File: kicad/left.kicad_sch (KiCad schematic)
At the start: 118 parts, among them Q1 PMF170XP,115, Q2 FS8205A_C2830320, SW1 TS-1088-AR02016, U1 TLV7031QDCKRQ1, U2 E73-2G4M08S1C, U3 SN74LVC1G74DQER, U4 S2B-PH-K-S(LF)(SN), U5 BL8573CS8TR, U6 DW01A_C42380662, U7 LP5024RSMR, X1 FC-13532.768KHZ9PF20PPM

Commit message: ...
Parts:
- added R17: RC0402FR-071ML, easyeda2kicad:R0402, symbol easyeda2kicad:RC0402FR-071ML
- added R18: WR04W2494FTL, easyeda2kicad:R0402, symbol easyeda2kicad:WR04W2494FTL
- S1, S10, S11, S12, S13, S14, S15, S16, S17, S18, S19, S2, S20, S3, S4, S5, S6, S7, S8, S9: footprint hexcaps:PG1350_hotswap -> hexcaps:PG1350_hotswap_reversed
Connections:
- net COL6 is gone; now on net LED_SCL: U2.17 (P1.09)
- net COL7 is gone; now on net STDBY: U2.1 (P1.11)
- net CHRG: now also U2.2 (P1.10); no longer U2.43 (NF2)
- net COL1: now also U2.32 (P0.20); no longer U2.38 (P1.02)
- net COL2: now also U2.34 (P0.22); no longer U2.36 (P1.00)
- net COL3: now also U2.36 (P1.00); no longer U2.34 (P0.22)
- net COL4: now also U2.38 (P1.02); no longer U2.32 (P0.20)
- net COL5: now also U2.40 (P1.04); no longer U2.6 (P1.13)
- net GND: now also R18.1
- net LED1: now also U7.8 (OUT7); no longer U7.17 (OUT16)
- net LED10: now also U7.18 (OUT17); no longer U7.7 (OUT6)
- net LED11: now also U7.22 (OUT21); no longer U7.3 (OUT2)
- net LED12: now also U7.5 (OUT4); no longer U7.20 (OUT19)
- net LED13: now also U7.11 (OUT10); no longer U7.14 (OUT13)
- net LED14: now also U7.19 (OUT18); no longer U7.6 (OUT5)
- net LED15: now also U7.23 (OUT22); no longer U7.2 (OUT1)
- net LED16: now also U7.4 (OUT3); no longer U7.21 (OUT20)
- net LED17: now also U7.10 (OUT9); no longer U7.15 (OUT14)
- net LED18: now also U7.20 (OUT19); no longer U7.5 (OUT4)
- net LED19: now also U7.24 (OUT23); no longer U7.1 (OUT0)
- net LED2: now also U7.14 (OUT13); no longer U7.11 (OUT10)
- net LED20: now also U7.1 (OUT0); no longer U7.24 (OUT23)
- net LED3: now also U7.15 (OUT14); no longer U7.10 (OUT9)
- net LED4: now also U7.7 (OUT6); no longer U7.18 (OUT17)
- net LED5: now also U7.13 (OUT12); no longer U7.12 (OUT11)
- net LED6: now also U7.17 (OUT16); no longer U7.8 (OUT7)
- net LED7: now also U7.21 (OUT20); no longer U7.4 (OUT3)
- net LED8: now also U7.6 (OUT5); no longer U7.19 (OUT18)
- net LED9: now also U7.12 (OUT11); no longer U7.13 (OUT12)
- net LED_EN: now also U2.15 (AI3); no longer U2.7 (AI0)
- net LED_SCL: no longer U2.9 (AI7)
- net LED_SDA: now also U2.16 (P0.08); no longer U2.8 (AI5)
- net PWR_BTN: now also R17.2
- net ROW1: now also U2.9 (AI7); no longer U2.28 (P15)
- net ROW3: now also U2.33 (P0.13); no longer U2.12 (P0.26)
- net ROW4: now also U2.42 (P1.06)
- net STDBY: no longer U2.41 (NF1)
- net SWBCLK: now also U2.37 (SWD); no longer U2.39 (SWC)
- net SWDIO: now also U2.39 (SWC); no longer U2.37 (SWD)
- net PWR_BTN_PRESS: now reaches U2.3 (P0.03)
- net PWR_BTN_PRESS: now also R17.1, R18.2

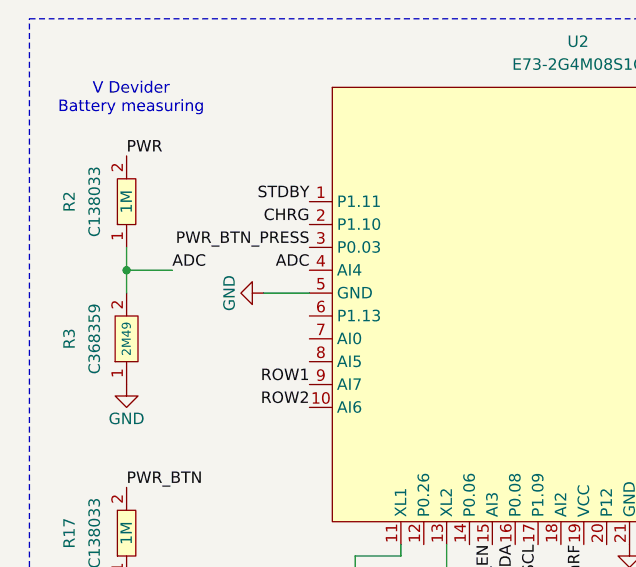
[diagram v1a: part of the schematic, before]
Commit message: left wiring done... right changed to shmitt inctead of comparator... need to do same on left... fixing of right in progress
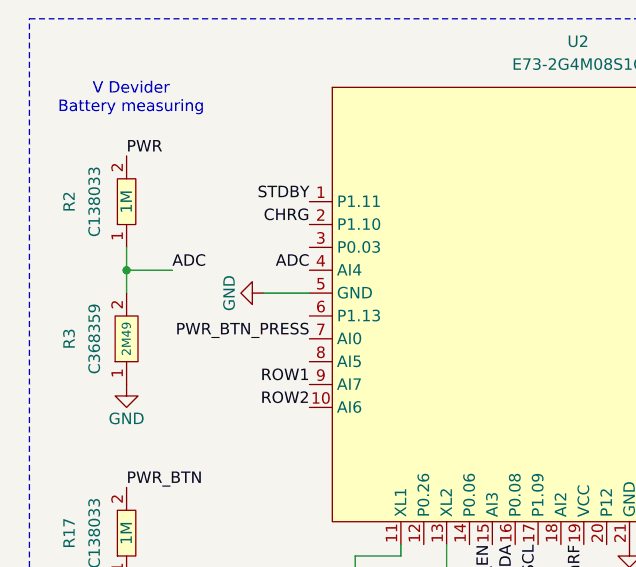
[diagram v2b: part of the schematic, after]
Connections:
- net PWR_BTN_PRESS: now also U2.7 (AI0); no longer U2.3 (P0.03)
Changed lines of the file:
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@@
+		)
+	)
+	(label "PWR_BTN_PRESS"
+		(at 45.72 123.19 180)
+		(effects
+			(font
+				(size 1.27 1.27)
+			)
+			(justify right bottom)
 		)
 	)
@@
 		(effects
 			(font
-				(size 1.27 1.27)
-			)
-			(justify right bottom)
-		)
-	)
-	(label "PWR_BTN_PRESS"
-		(at 45.72 113.03 180)
-		(effects
-			(font

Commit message: pcb done. schematick done. need to double check schematick and ask in discord about pcb... but else done
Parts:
- removed R5: RC0402FR-074M3L, :R0402, symbol easyeda2kicad:RC0402FR-074M3L
- removed R6: RC0402FR-071ML, easyeda2kicad:R0402, symbol easyeda2kicad:RC0402FR-071ML
- removed U1: TLV7031QDCKRQ1, :SC-70-5_L2.0-W1.3-P0.65-LS2.1-BR, symbol easyeda2kicad:TLV7031QDCKRQ1
- added U1: SN74LVC1G17DBVR, easyeda2kicad:SOT-23-5_L3.0-W1.7-P0.95-LS2.8-BR, symbol easyeda2kicad:SN74LVC1G17DBVR
- renumbered R17 to R4, R18 to R5, R4 to R6
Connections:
- net GND: now also U1.3 (GND)
- net PWR_BTN: now also U1.5 (VCC)
- net at C2.1, D1.2, R6.2: now also U1.2 (A)
- net at U3.1 (CLK): now also U1.4 (Y)
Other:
- moved on the sheet: U3

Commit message: text position changes
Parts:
- removed R6: WR04W2494FTL, easyeda2kicad:R0402, symbol easyeda2kicad:WR04W2494FTL
- added R6: 0402WGF1604TCE, easyeda2kicad:R0402, symbol easyeda2kicad:0402WGF1604TCE
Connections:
- net PWR_BTN: now also R6.1
- net at C2.1, D1.2, U1.2 (A): now also R6.2
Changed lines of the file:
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@@
 	)
 	(symbol
-		(lib_id "easyeda2kicad:WR04W2494FTL")
-		(at 36.83 39.37 0)
-		(unit 1)
-		(exclude_from_sim no)
-		(in_bom yes)
-		(on_board yes)
-		(dnp no)
-		(property "Reference" "R6"
-			(at 36.83 33.02 0)
-			(effects
-				(font
-					(size 1.27 1.27)
-				)
-			)
-		)
-		(property "Value" "WR04W2494FTL"
-			(at 36.83 35.56 0)
-			(effects
-				(font
-					(size 1.27 1.27)
-				)
-				(hide yes)
-			)
-		)
-		(property "Footprint" "easyeda2kicad:R0402"
-			(at 36.83 46.99 0)
-			(effects
-				(font
-					(size 1.27 1.27)
-				)
-				(hide yes)
-			)
-		)
-		(property "Datasheet" "https://lcsc.com/product-detail/Others_Walsin-Tech-Corp-WR04W2494FTL_C368359.html"
-			(at 36.83 49.53 0)
-			(effects
-				(font
-					(size 1.27 1.27)
-				)
-				(hide yes)
-			)
-		)
-		(property "Description" "2M49"
-			(at 36.83 39.37 0)
-			(effects
-				(font
-					(size 1 1)
-				)
-			)
-		)
-		(property "LCSC Part" "C368359"
-			(at 36.83 35.814 0)
-			(effects
-				(font
-					(size 1.27 1.27)
-				)
-			)
-		)
-		(pin "1"
-		)
-		(pin "2"
-		)
-		(instances
-			(project ""
-				(path "/3171f1b4-f2dd-4471-8b63-415e18370dba"
-					(reference "R6")
-					(unit 1)
-				)
-			)
-		)
-	)
-	(symbol
 		(lib_id "PCM_SparkFun-PowerSymbol:GND")
 		(at 168.91 35.56 270)
@@
 					(unit 1)
 				)
+			)
+		)
+	)
+	(symbol
+		(lib_id "easyeda2kicad:0402WGF1604TCE")
+		(at 36.83 39.37 0)
+		(unit 1)
+		(exclude_from_sim no)
+		(in_bom yes)
+		(on_board yes)
+		(dnp no)
+		(property "Reference" "R6"
+			(at 36.83 36.83 0)
+			(effects
+				(font
+					(size 1.27 1.27)
+				)
+			)
+		)
+		(property "Value" "0402WGF1604TCE"
+			(at 36.83 35.56 0)
+			(effects
+				(font
+					(size 1.27 1.27)
+				)
+				(hide yes)
+			)
+		)
+		(property "Footprint" "easyeda2kicad:R0402"
+			(at 36.83 46.99 0)
+			(effects
+				(font
+					(size 1.27 1.27)
+				)
+				(hide yes)
+			)
+		)
+		(property "Datasheet" "https://lcsc.com/product-detail/Chip-Resistor-Surface-Mount_Uniroyal-Elec-0402WGF1604TCE_C423231.html"
+			(at 36.83 49.53 0)
+			(effects
+				(font
+					(size 1.27 1.27)
+				)
+				(hide yes)
+			)
+		)
+		(property "Description" "3M48"
+			(at 36.83 39.37 0)
+			(effects
+				(font
+					(size 1.016 1.016)
+				)
+			)
+		)
+		(property "LCSC Part" "C423231"
+			(at 36.83 52.07 0)
+			(effects
+				(font
+					(size 1.27 1.27)
+				)
+				(hide yes)
+			)
+		)
+		(pin "2"
+		)
+		(pin "1"
+		)
+		(instances
+			(project "left"
+				(path "/3171f1b4-f2dd-4471-8b63-415e18370dba"
+					(reference "R6")
+					(unit 1)
+				)

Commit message: checked and update schematics on off need to update it in pcb...
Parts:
- removed R1: RC0402FR-07100KL, easyeda2kicad:R0402, symbol easyeda2kicad:RC0402FR-07100KL
- added C4: GRM033C71C104KE14D, easyeda2kicad:C0201, symbol easyeda2kicad:GRM033C71C104KE14D
- added R5, R7: RC0402FR-07100KL, easyeda2kicad:R0402, symbol easyeda2kicad:RC0402FR-07100KL
- renumbered C9 to C10, C10 to C11, C11 to C12, C12 to C13, C13 to C14, C14 to C15, C15 to C16, C16 to C17, C17 to C18, C18 to C19, C19 to C20, C20 to C21, C21 to C22, C22 to C23, C23 to C24, C24 to C25, C25 to C26, C26 to C27, C27 to C28, C4 to C5, C5 to C6, C6 to C7, C7 to C8, C8 to C9, R2 to R1, R9 to R10, R10 to R11, R11 to R12, R12 to R13, R13 to R14, R14 to R15, R15 to R16, R16 to R17, R3 to R2, R4 to R3, R5 to R4, R7 to R8, R8 to R9
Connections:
- net BAT+: now also U1.5 (VCC), R7.2; no longer U3.6 (~{CLR})
- net GND: now also C4.1, R5.2
- net PWR_BTN: now also R5.1; no longer U1.5 (VCC)
- new net: C4.2, R7.1, U3.6 (~{CLR})
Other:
- moved on the sheet: C2, D1, U1, U3

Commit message: .
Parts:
- removed C10, C11, C12, C13, C14, C15, C16, C17, C18, C19, C20, C21, C22, C23, C24, C25, C26, C7, C8, C9: GRM033C71C104KE14D, easyeda2kicad:C0201, symbol easyeda2kicad:GRM033C71C104KE14D
- removed C6: GRM188C71C475KE21D, easyeda2kicad:C0603, symbol easyeda2kicad:GRM188C71C475KE21D
- removed R7: RC0402FR-07100KL, easyeda2kicad:R0402, symbol easyeda2kicad:RC0402FR-07100KL
- added C6: ZRB15XR61A475KE01D, easyeda2kicad:C0402, symbol easyeda2kicad:ZRB15XR61A475KE01D
- added R18: RC0402FR-0710KL, easyeda2kicad:R0402, symbol easyeda2kicad:RC0402FR-0710KL
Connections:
- net BAT+: now also R18.2
- net GND: now also C6.2
- net VBUS: now also C6.1
- net at C4.2, U3.6 (~{CLR}): now also R18.1

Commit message: .
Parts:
- removed C6: ZRB15XR61A475KE01D, easyeda2kicad:C0402, symbol easyeda2kicad:ZRB15XR61A475KE01D
- removed R18: RC0402FR-0710KL, easyeda2kicad:R0402, symbol easyeda2kicad:RC0402FR-0710KL
- removed R3: RC0402FR-071ML, easyeda2kicad:R0402, symbol easyeda2kicad:RC0402FR-071ML
- removed R4: WR04W2494FTL, easyeda2kicad:R0402, symbol easyeda2kicad:WR04W2494FTL
- removed R5: RC0402FR-07100KL, easyeda2kicad:R0402, symbol easyeda2kicad:RC0402FR-07100KL
- added C5: ZRB15XR61A475KE01D, easyeda2kicad:C0402, symbol easyeda2kicad:ZRB15XR61A475KE01D
- added C9: GRM033C71C104KE14D, easyeda2kicad:C0201, symbol easyeda2kicad:GRM033C71C104KE14D
- added R3: RC0402FR-07100KL, easyeda2kicad:R0402, symbol easyeda2kicad:RC0402FR-07100KL
- added R4, R7: RC0402FR-0710KL, easyeda2kicad:R0402, symbol easyeda2kicad:RC0402FR-0710KL
- added U8: MAX17048, PCM_SparkFun-Semiconductor-Standard:DFN-8_2x2mm_P0.5mm_EP1.2x0.8mm, symbol PCM_SparkFun-IC-Power:MAX17048
- S1, S10, S11, S12, S13, S14, S15, S16, S17, S18, S19, S2, S20, S3, S4, S5, S6, S7, S8, S9: footprint hexcaps:PG1350_hotswap_reversed -> hexcaps:PG1350_hotswap
- renumbered C5 to C6, C27 to C7, C28 to C8
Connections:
- net BAT+: now also C9.1, R7.2, U8.2 (CELL), U8.3 (VDD)
- net CHRG: now also U2.41 (NF1); no longer U2.2 (P1.10)
- net COL1: now also U2.38 (P1.02); no longer U2.32 (P0.20)
- net COL2: now also U2.36 (P1.00); no longer U2.34 (P0.22)
- net COL3: now also U2.34 (P0.22); no longer U2.36 (P1.00)
- net COL4: now also U2.32 (P0.20); no longer U2.38 (P1.02)
- net COL5: now also U2.6 (P1.13); no longer U2.40 (P1.04)
- net GND: now also C5.2, C9.2, R3.2, U8.1 (CTG), U8.4 (GND), U8.6 (QSTRT), U8.9 (GND)
- net LED1: now also U7.17 (OUT16); no longer U7.8 (OUT7)
- net LED10: now also U7.7 (OUT6); no longer U7.18 (OUT17)
- net LED11: now also U7.3 (OUT2); no longer U7.22 (OUT21)
- net LED12: now also U7.20 (OUT19); no longer U7.5 (OUT4)
- net LED13: now also U7.14 (OUT13); no longer U7.11 (OUT10)
- net LED14: now also U7.6 (OUT5); no longer U7.19 (OUT18)
- net LED15: now also U7.2 (OUT1); no longer U7.23 (OUT22)
- net LED16: now also U7.21 (OUT20); no longer U7.4 (OUT3)
- net LED17: now also U7.15 (OUT14); no longer U7.10 (OUT9)
- net LED18: now also U7.5 (OUT4); no longer U7.20 (OUT19)
- net LED19: now also U7.1 (OUT0); no longer U7.24 (OUT23)
- net LED2: now also U7.11 (OUT10); no longer U7.14 (OUT13)
- net LED20: now also U7.22 (OUT21); no longer U7.1 (OUT0)
- net LED3: now also U7.10 (OUT9); no longer U7.15 (OUT14)
- net LED4: now also U7.18 (OUT17); no longer U7.7 (OUT6)
- net LED5: now also U7.12 (OUT11); no longer U7.13 (OUT12)
- net LED6: now also U7.8 (OUT7); no longer U7.17 (OUT16)
- net LED7: now also U7.4 (OUT3); no longer U7.21 (OUT20)
- net LED8: now also U7.19 (OUT18); no longer U7.6 (OUT5)
- net LED9: now also U7.13 (OUT12); no longer U7.12 (OUT11)
- net PWR: no longer R1.2
- net PWR_BTN: now also R1.2, R3.1
- net PWR_BTN_PRESS: now also R1.1, R2.2, U2.30 (P17); no longer U2.7 (AI0)
- net ROW1: now also U2.28 (P15); no longer U2.9 (AI7)
- net ROW3: now also U2.12 (P0.26); no longer U2.33 (P0.13)
- net ROW4: now also U2.9 (AI7); no longer U2.42 (P1.06)
- net STDBY: now also U2.43 (NF2); no longer U2.1 (P1.11)
- net SWBCLK: now also U2.39 (SWC); no longer U2.37 (SWD)
- net SWDIO: now also U2.37 (SWD); no longer U2.39 (SWC)
- net VBUS: now also C5.1
- net VDD_nRF: now also R4.2
- net at C4.2, U3.6 (~{CLR}): now also R7.1
- net BAT_ALTR: now reaches U2.18 (AI2)
- net BAT_ALTR: now also R4.1, U8.5 (~{ALRT})
- removed net ADC: R1.1, R2.2, U2.4 (AI4)
- net LED_SCL renamed SCL
- net SCL: now also U8.7 (SCL)
- net LED_SDA renamed SDA
- net SDA: now also U8.8 (SDA)
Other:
- moved on the sheet: C1, C2, C3, C4, C6, C7, C8, D1, D10, D11, D12, D13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
